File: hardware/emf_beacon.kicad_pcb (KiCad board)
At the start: 2 copper layers, 100 x 100 mm, 134 parts, among them J1 USB_C_Receptacle_USB2.0_16P, J10 Conn_01x02, J11 Conn_01x02, J12 Conn_01x02, J13 Conn_01x02, J14 Conn_01x02, J2 Conn_01x06, J3 Conn_01x06, J4 Conn_01x02, J5 Conn_01x02, J6 Conn_01x02, J7 Conn_01x02, J8 Conn_01x02, J9 Conn_01x02, Q1 AO3400A, Q10 AO3400A, Q11 AO3400A, Q12 DMP3013SFV, Q2 AO3400A, Q3 AO3400A, Q4 AO3400A, Q5 AO3400A, Q6 AO3400A, Q7 AO3400A, Q8 AO3400A, Q9 AO3400A, SW1 SW_DIP_x10, SW2 SW_Push, U1 ESP32-C3-WROOM-02, U2 MCP23017T-E/SS, U3 CA-IS3092W, U4 PCA9685PW, U5 TPS565208, U7 TPS82140SILR

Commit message: general schematic and PCB clean
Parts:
- J14: footprint Connector_Phoenix_MSTB:PhoenixContact_MSTBVA_2,5_2-G-5,08_1x02_P5.08mm_Vertical -> TerminalBlock_WAGO:TerminalBlock_WAGO_2601-3102_1x02_P3.50mm_Vertical
- J2, J3: value Conn_01x06 -> B6B-PH-SM4-TB
- SW1: footprint Button_Switch_THT:SW_DIP_SPSTx10_Slide_6.7x26.96mm_W7.62mm_P2.54mm_LowProfile -> Button_Switch_THT:SW_DIP_SPSTx10_Slide_9.78x27.58mm_W7.62mm_P2.54mm
- U4: value PCA9685PW -> PCA9685PW,118
- moved H1 2.50 mm to (181.8, 68.2)
- moved H4 2.50 mm to (118.2, 68.2)
- moved H3 2.50 mm to (118.2, 131.8)
- moved H2 2.50 mm to (181.8, 131.8)
- moved J14 2.36 mm to (131.8, 135.5), turned to 180 degrees
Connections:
- J2 pad MP: (no net) -> GND_ISO
- J3 pad MP: (no net) -> GND_ISO
- SW1 pad 11: /CTRL/WIFI_~{ENABLE} -> /DMX512/WIFI_~{ENABLE}
- U1 pad 4: /CTRL/WIFI_~{ENABLE} -> unconnected-(U1-IO5-Pad4)
- U2 pad 3: unconnected-(U2-GPB2-Pad3) -> /DMX512/WIFI_~{ENABLE}
- U3 pad 7: unconnected-(U3-PV-Pad7) -> +3V3

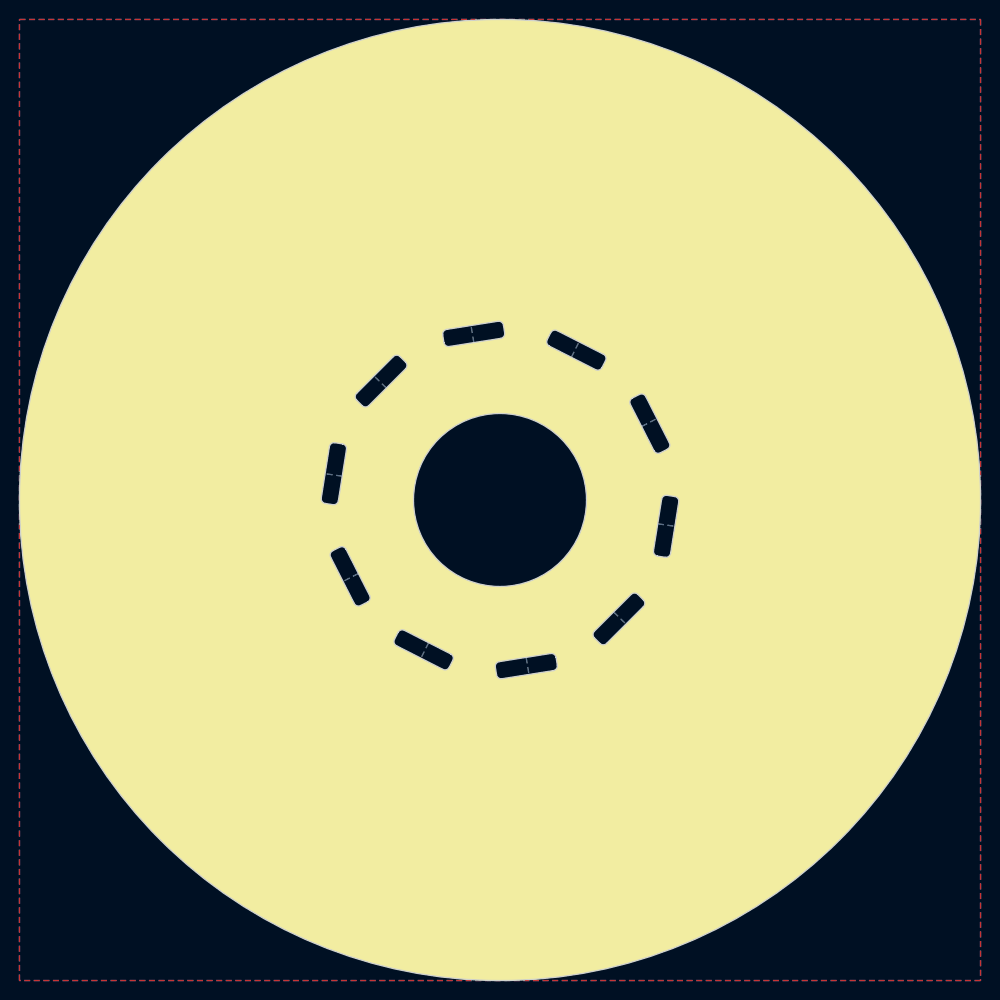
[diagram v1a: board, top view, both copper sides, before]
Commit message: sorting button and LED
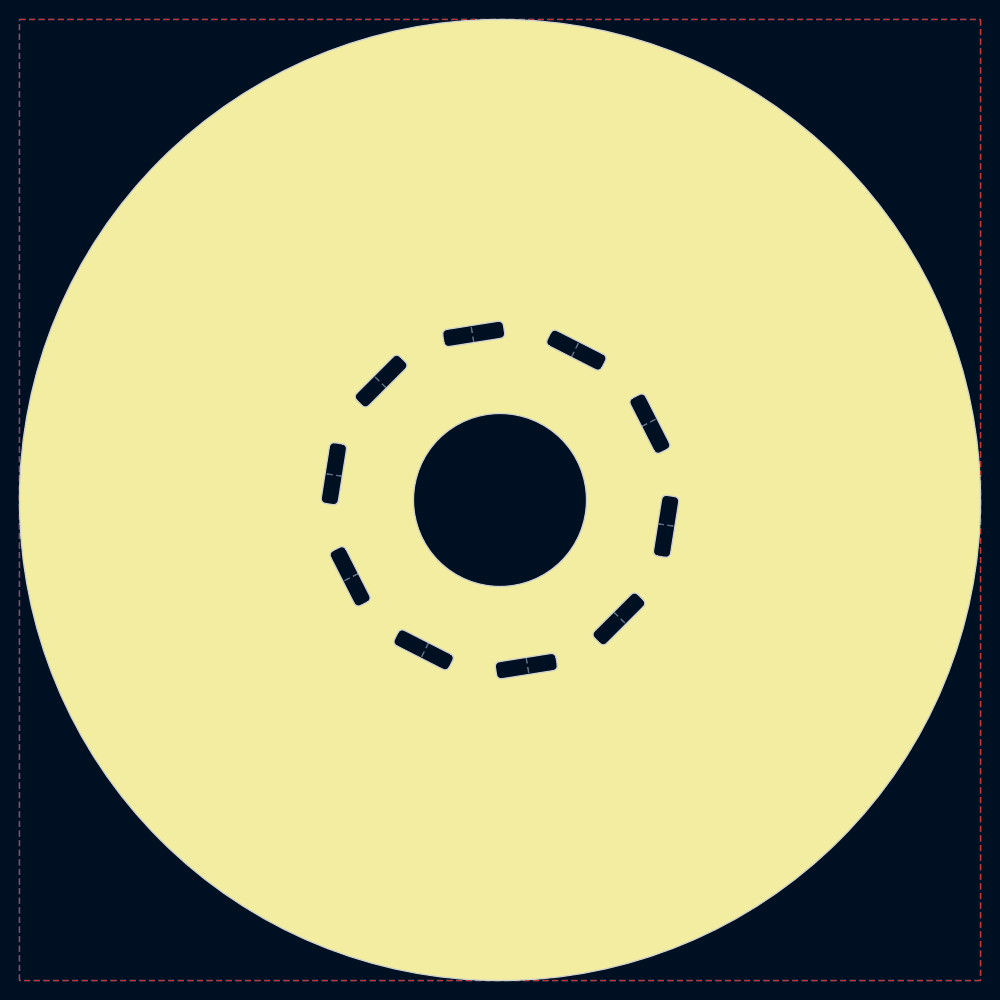
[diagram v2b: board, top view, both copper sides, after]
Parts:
- removed R42: 10k, Resistor_SMD:R_0603_1608Metric
- added R27: 10k, Resistor_SMD:R_0603_1608Metric, B.Cu at (126.2, 67.8)
- added R28: 470R, Resistor_SMD:R_0603_1608Metric, B.Cu at (167.4, 69.6)
- D5: value SS34 -> B16WS; footprint Diode_SMD:D_SMA -> Diode_SMD:D_SOD-323
- R40: value R -> 2k7
- SW2: value SW_Push -> TS-1088-AR02016; footprint Button_Switch_SMD:SW_SPST_B3U-1000P -> Button_Switch_SMD:SW_Push_SPST_NO_Alps_SKRK
- moved LED1 37.5 mm to (173.0, 68.5)
- moved R40 37.5 mm to (173.0, 71.0)
- moved R18 10.9 mm to (140.0, 121.8), turned to 63 degrees
- moved R16 10.7 mm to (167.5, 115.8), turned to 135 degrees
- moved R20 10.4 mm to (126.5, 97.5), turned to -9 degrees
- moved R25 10.3 mm to (173.8, 102.5), turned to 171 degrees
- moved R24 10.3 mm to (170.8, 88.2), turned to -153 degrees
- moved R19 10.3 mm to (129.5, 111.8), turned to 27 degrees
- moved C7 8.73 mm to (161.5, 131.2)
- moved C8 8.73 mm to (163.5, 131.2)
- moved U3 8.63 mm to (170.8, 135.0)
- moved R17 8.50 mm to (154.8, 123.5), turned to 99 degrees
- moved C16 6.86 mm to (180.8, 116.8)
- moved Q4 5.22 mm to (128.5, 109.2), turned to 27 degrees
- moved Q10 5.22 mm to (172.8, 105.0), turned to 171 degrees
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- renumbered TP6 to TP5
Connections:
- net /CTRL/I2C_SCL renamed /I2C_SCL
- net /CTRL/I2C_SDA renamed /I2C_SDA
- net /CTRL/I2C_~{INT} renamed /I2C_~{INT}
- C27 pad 1: /CTRL/ESP_~{BOOT} -> Net-(D6-A)
- D6 pad 2: /CTRL/ESP_~{BOOT} -> Net-(D6-A)
- LED1 pad 1: GND -> /CTRL/STATUS_LEDn
- R40 pad 1: unconnected-(R40-Pad1) -> +3V3
- U1 pad 7: Net-(U1-IO8) -> /CTRL/STATUS_LEDn
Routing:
- net /CTRL/USB-: track 0.00 -> 12.2 mm
- net /CTRL/USB+: track 0.00 -> 11.8 mm
- net /DMX512/WIFI_~{ENABLE}: track 0.00 -> 10.2 mm
- net Net-(J4-Pin_2): track 2.74 -> 0.00 mm
- net +3V3: track 16.0 -> 13.3 mm, vias 4 -> 3
- net Net-(U1-IO8): track 2.43 -> 0.00 mm
- net /CTRL/STATUS_LEDn: track 0.00 -> 2.43 mm
- net /CTRL/ESP_~{RST}: track 20.2 -> 20.8 mm

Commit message: starting layout
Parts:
- moved R4 50.4 mm to (188.8, 73.5), turned to 0 degrees
- moved R5 50.1 mm to (188.8, 75.0), turned to 0 degrees
- moved C40 38.8 mm to (120.0, 78.5), turned to 180 degrees
- moved R54 35.6 mm to (124.2, 80.8), turned to -90 degrees
- moved R55 35.6 mm to (124.2, 83.8), turned to -90 degrees
- moved U7 33.5 mm to (121.5, 81.5), turned to 0 degrees
- moved C22 32.1 mm to (114.2, 81.5), turned to 90 degrees
- moved C20 31.9 mm to (118.2, 81.5), turned to 90 degrees
- moved C21 31.7 mm to (116.2, 81.5), turned to 90 degrees
- moved C39 29.1 mm to (121.8, 84.2), turned to 180 degrees
- moved C15 26.0 mm to (119.5, 118.0)
- moved R13 24.6 mm to (194.0, 83.8), turned to 90 degrees
- moved R6 22.9 mm to (135.8, 59.5), turned to 90 degrees
- moved C4 22.9 mm to (138.8, 59.5)
- moved R7 22.8 mm to (137.2, 59.5)
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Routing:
- net VDC: track 2.67 -> 97.4 mm, vias 0 -> 2
- net +3V3: track 13.3 -> 29.0 mm, vias 3 -> 4
- net Net-(D5-A): track 0.00 -> 14.4 mm, vias 0 -> 2
- net /DMX512/DMX_ADDR7: track 2.68 -> 16.5 mm
- net /DMX512/DMX_ADDR0: track 18.2 -> 27.6 mm, vias 1 -> 0
- net /DMX512/DMX_ADDR1: track 16.5 -> 24.8 mm, vias 1 -> 0
- net /CTRL/USB-: track 12.2 -> 19.9 mm
- net /CTRL/USB+: track 11.8 -> 19.3 mm
- net /DMX512/DMX_ADDR2: track 14.8 -> 22.0 mm, vias 1 -> 0
- net /DMX512/DMX_ADDR8: track 7.59 -> 13.8 mm
- net /DMX512/DMX_ADDR3: track 13.0 -> 19.2 mm, vias 1 -> 0
- net Net-(U2-~{RESET}): track 0.00 -> 5.62 mm
- net /CTRL/VCC_MON: track 0.00 -> 5.61 mm
- net /I2C_SDA: track 38.2 -> 42.8 mm, vias 0 -> 1
- net /I2C_SCL: track 36.4 -> 40.8 mm, vias 0 -> 1
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- added copper zone on B.Cu, net +3V3
- added copper zone on B.Cu, net GND_ISO
- added copper zone on F.Cu, net GND_ISO
- added copper zone on B.Cu, net VDC
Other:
- board text added: "Aim for 8mm gap between GND and GND_ISO"
- board text added: "WiFi 255 128 D 64 M 32 X 16 8 A 4 d 2 d 1 r"

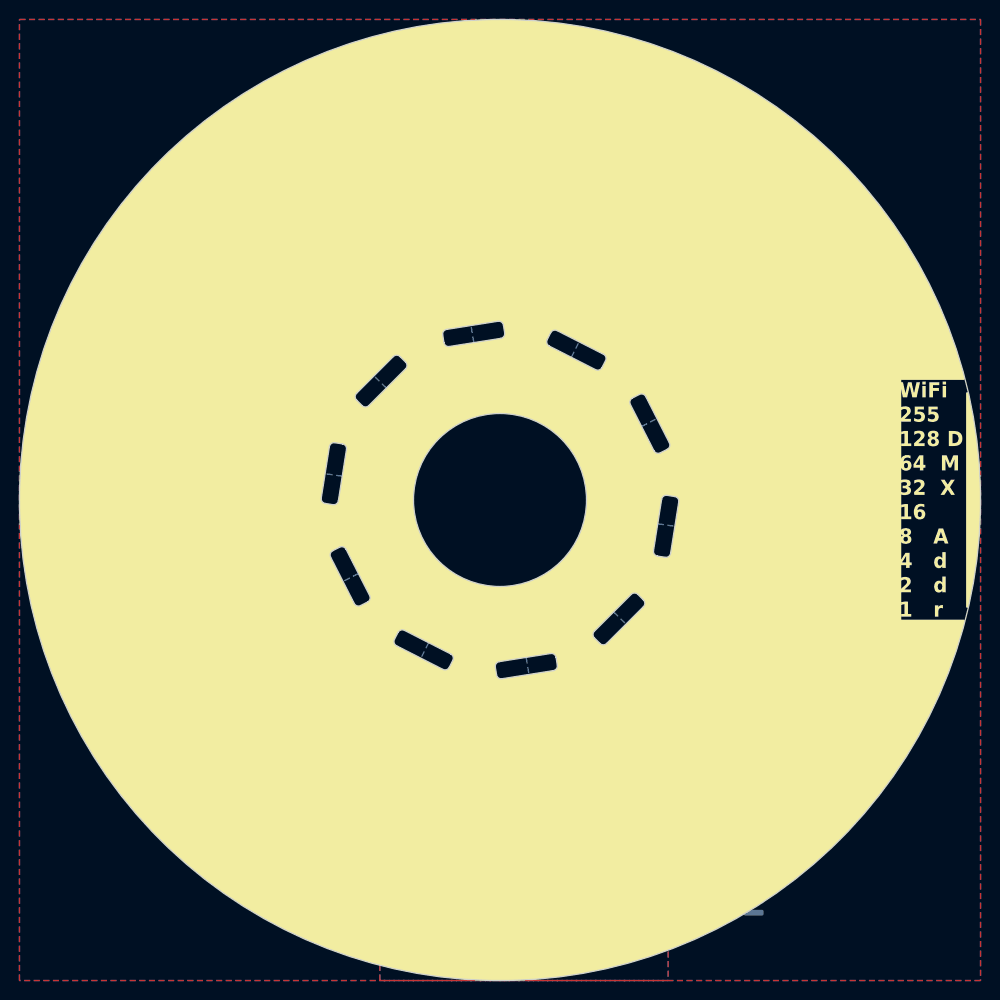
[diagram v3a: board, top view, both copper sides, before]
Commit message: adding DRU for DMX isolation
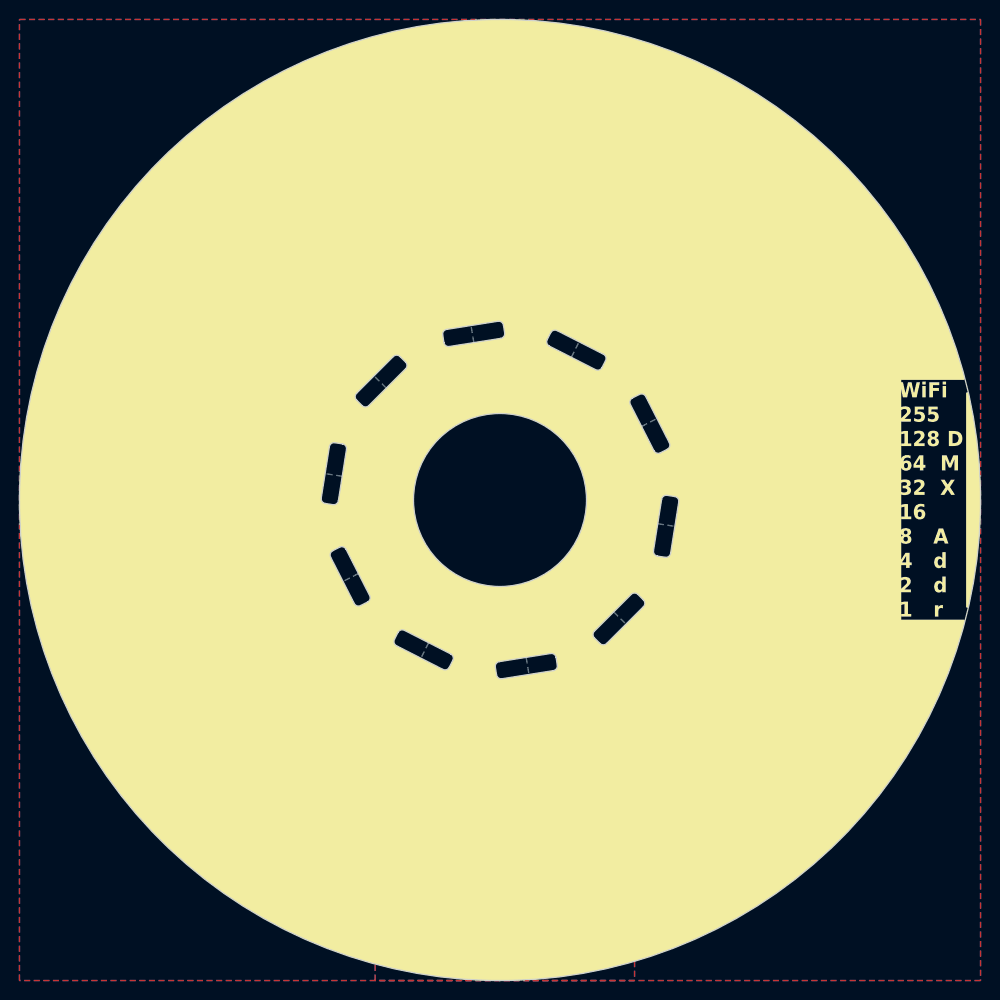
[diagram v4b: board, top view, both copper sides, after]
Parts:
- removed U3: CA-IS3092W, Package_SO:SOIC-16W_7.5x10.3mm_P1.27mm
- added C23: 100nF, Capacitor_SMD:C_0603_1608Metric, B.Cu at (161.0, 131.0)
- added TP6: TestPoint, TestPoint:TestPoint_Pad_D1.5mm, B.Cu at (103.5, 99.5)
- added TP7: TestPoint, TestPoint:TestPoint_Pad_D1.5mm, B.Cu at (176.5, 109.5)
- added U6: CA-IS3092VW, Package_SO:SOIC-16W_7.5x10.3mm_P1.27mm, B.Cu at (165.8, 137.5)
- R10, R11: value 4.7k -> 4k7
- moved TP5 50.7 mm to (125.8, 77.5)
- moved R29 22.0 mm to (113.0, 89.8), turned to 0 degrees
- moved R30 20.7 mm to (113.0, 91.2), turned to 180 degrees
- moved C12 19.9 mm to (117.0, 91.2), turned to 0 degrees
- moved R8 18.8 mm to (157.5, 144.8), turned to 0 degrees
- moved C18 18.6 mm to (116.8, 109.8), turned to -90 degrees
- moved C5 16.6 mm to (157.5, 147.2), turned to 0 degrees
- moved C19 16.2 mm to (113.2, 109.8), turned to -90 degrees
- moved U5 15.0 mm to (115.0, 94.2), turned to 90 degrees
- moved D3 13.7 mm to (128.0, 118.0), turned to 0 degrees
- moved C17 13.5 mm to (110.0, 95.0), turned to 90 degrees
- moved R15 13.3 mm to (162.5, 75.2)
- moved C11 13.0 mm to (164.5, 75.0)
- moved C13 13.0 mm to (112.0, 95.0), turned to 90 degrees
- moved TP3 12.1 mm to (108.8, 113.2), turned to 180 degrees
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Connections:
- net /POWER/LED_~{PGD} renamed /CTRL/LED_~{PGD}
- net Net-(J2-Pin_6) renamed /DMX512/DMX_SHLD
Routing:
- net +3V3: track 29.0 -> 177.6 mm, vias 4 -> 7
- net /CTRL/DMX_DE/~{RE}: track 2.43 -> 94.9 mm
- net /CTRL/DMX_TX: track 0.00 -> 80.8 mm
- net /CTRL/DMX_RX: track 0.00 -> 79.3 mm
- net /I2C_~{INT}: track 6.70 -> 35.1 mm, vias 0 -> 1
- net /CTRL/STATUS_LEDn: track 2.43 -> 21.0 mm
- net /CTRL/LED_~{OE}: track 2.43 -> 16.5 mm
- net GND_ISO: track 9.00 -> 0.00 mm, vias 1 -> 2
- net /I2C_SCL: track 40.8 -> 49.1 mm, vias 1 -> 2
- net /I2C_SDA: track 42.8 -> 51.1 mm, vias 1 -> 2
- net Net-(U5-SW): track 0.00 -> 8.01 mm, vias 0 -> 2
- net /CTRL/ESP_~{BOOT}: track 8.56 -> 2.53 mm
- net /DMX512/DMX_DATA-: track 9.56 -> 14.7 mm
- net /DMX512/DMX_DATA+: track 9.56 -> 14.7 mm
- net Net-(D6-A): track 0.00 -> 4.98 mm
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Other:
- board text removed: "Aim for 8mm gap between GND and GND_ISO"

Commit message: more layout and fixing OOS items
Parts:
- removed Q11: AO3400A, Package_TO_SOT_SMD:SOT-23
- removed R31: 100R, Resistor_SMD:R_0603_1608Metric
- removed R32, R33: 10k, Resistor_SMD:R_0603_1608Metric
- J10, J11, J12, J13, J4, J5, J6, J7, J8, J9: footprint Pinski1_parts:LED_Stick -> emf_beacon_library:LED_Stick
- J14: footprint TerminalBlock_WAGO:TerminalBlock_WAGO_2601-3102_1x02_P3.50mm_Vertical -> emf_beacon_library:MX250-3.5-02P-A-GY01-Cu-A
- L1: value MDE0840-3R3M -> MWSA0804S-3R3MT
- moved TP7 21.5 mm to (158.5, 121.2)
- moved C11 15.2 mm to (175.5, 85.5), turned to 0 degrees
- moved C9 9.65 mm to (172.8, 133.8)
- moved C10 9.58 mm to (174.5, 133.8)
- moved R15 8.22 mm to (170.2, 72.5)
- moved R11 7.00 mm to (157.2, 135.0)
- moved C16 2.30 mm to (172.0, 113.5), turned to -45 degrees
- moved R8 2.12 mm to (159.0, 146.2), turned to -90 degrees
- moved J14 1.83 mm to (129.8, 136.9), turned to 0 degrees
- moved C14 1.46 mm to (128.5, 128.8), turned to 180 degrees
- moved C5 1.41 mm to (156.5, 146.2), turned to -90 degrees
- moved C23 1.00 mm to (162.0, 131.0)
- moved C7 0.53 mm to (157.1, 132.8)
- moved C8 0.53 mm to (158.8, 133.0)
- moved R10 0.25 mm to (157.2, 140.0)
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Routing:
- net +3V3: track 177.6 -> 227.2 mm, vias 7 -> 11
- net /CTRL/DMX_DE/~{RE}: track 94.9 -> 113.0 mm
- net /CTRL/DMX_RX: track 79.3 -> 96.8 mm, vias 0 -> 2
- net /CTRL/DMX_TX: track 80.8 -> 96.9 mm
- net /DMX512/DMX_SHLD: track 9.00 -> 16.4 mm
- net /DMX512/DMX_DATA-: track 14.7 -> 19.6 mm
- net /DMX512/DMX_DATA+: track 14.7 -> 19.6 mm
- net +6V5: track 36.1 -> 40.8 mm
- net Net-(Q11-G): track 3.36 -> 0.00 mm
- net /LEDS/LED8: track 0.00 -> 2.09 mm
- net /LEDS/LED9: track 0.00 -> 2.05 mm
- net /CTRL/LED_~{PGD}: track 1.74 -> 0.00 mm
- net /I2C_SDA: track 51.1 -> 52.5 mm
- net /I2C_SCL: track 49.1 -> 50.6 mm
- net GND_ISO: vias 2 -> 15
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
